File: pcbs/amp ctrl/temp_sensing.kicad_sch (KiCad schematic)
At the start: 8 parts, among them J89 Conn_02x02, U67 ADC081C021

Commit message: Spring connector layout updates
Amp ctrl: added spring connectors for current sense, thermistors, +5V regulator
Amp ctrl: changed pass-through screwdriver holes to mounting holes
Amp ctrl: added part number to optional level shifter
Amp pwr: marked DNP components as DNP
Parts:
- added J116: Conn_01x02, shim:Conn_70AAJ-M_SIB_1x02_P2.54mm_F_bare, symbol Connector_Generic:Conn_01x02
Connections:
- net at C205.2, C207.2, J89.4 (Pin_4)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: now also J116.2 (Pin_2)
- net at C206.2, J89.2 (Pin_2), R267.1: now also J116.1 (Pin_1)
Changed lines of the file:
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@@
 		(exclude_from_sim no)
 		(at 106.68 133.35 0)
-		(size 83.82 27.94)
+		(size 83.82 30.5285)
 		(margins 0.9525 0.9525 0.9525 0.9525)
 		(stroke
@@
 	)
 	(junction
+		(at 100.33 95.25)
+		(diameter 0)
+		(color 0 0 0 0)
+	)
+	(junction
 		(at 181.61 77.47)
 		(diameter 0)
@@
 	)
 	(junction
+		(at 97.79 92.71)
+		(diameter 0)
+		(color 0 0 0 0)
+	)
+	(junction
 		(at 127 95.25)
 		(diameter 0)
@@
 	(wire
 		(pts
-			(xy 93.98 92.71) (xy 127 92.71)
+			(xy 91.44 101.6) (xy 97.79 101.6)
+		)
+		(stroke
+			(width 0)
+			(type default)
+		)
+	)
+	(wire
+		(pts
+			(xy 93.98 92.71) (xy 97.79 92.71)
 		)
 		(stroke
@@
 		)
 	)
+	(wire
+		(pts
+			(xy 97.79 101.6) (xy 97.79 92.71)
+		)
+		(stroke
+			(width 0)
+			(type default)
+		)
+	)
+	(wire
+		(pts
+			(xy 100.33 95.25) (xy 127 95.25)
+		)
+		(stroke
+			(width 0)
+			(type default)
+		)
+	)
 	(polyline
 		(pts
@@
 	(wire
 		(pts
-			(xy 93.98 95.25) (xy 127 95.25)
+			(xy 93.98 95.25) (xy 100.33 95.25)
 		)
 		(stroke
@@
 	(wire
 		(pts
+			(xy 100.33 104.14) (xy 100.33 95.25)
+		)
+		(stroke
+			(width 0)
+			(type default)
+		)
+	)
+	(wire
+		(pts
 			(xy 181.61 77.47) (xy 181.61 76.2)
 		)
@@
 		(pts
 			(xy 142.24 102.87) (xy 142.24 116.84)
+		)
+		(stroke
+			(width 0)
+			(type default)
+		)
+	)
+	(wire
+		(pts
+			(xy 91.44 104.14) (xy 100.33 104.14)
+		)
+		(stroke
+			(width 0)
+			(type default)
+		)
+	)
+	(wire
+		(pts
+			(xy 97.79 92.71) (xy 127 92.71)
 		)
 		(stroke
@@
 					(unit 1)
 				)
+			)
+		)
+	)
+	(symbol
+		(lib_id "Connector_Generic:Conn_01x02")
+		(at 86.36 101.6 0)
+		(mirror y)
+		(unit 1)
+		(body_style 1)
+		(exclude_from_sim no)
+		(in_bom no)
+		(on_board yes)
+		(in_pos_files no)
+		(dnp no)
+		(property "Reference" "J116"
+			(at 83.82 101.5999 0)
+			(show_name no)
+			(do_not_autoplace no)
+			(effects
+				(font
+					(size 1.27 1.27)
+				)
+				(justify left)
+			)
+		)
+		(property "Value" "Conn_01x02"
+			(at 83.82 104.1399 0)
+			(hide yes)
+			(show_name no)
+			(do_not_autoplace no)
+			(effects
+				(font
+					(size 1.27 1.27)
+				)
+				(justify left)
+			)
+		)
+		(property "Footprint" "shim:Conn_70AAJ-M_SIB_1x02_P2.54mm_F_bare"
+			(at 86.36 101.6 0)
+			(hide yes)
+			(show_name no)
+			(do_not_autoplace no)
+			(effects
+				(font
+					(size 1.27 1.27)
+				)
+			)
+		)
+		(property "Datasheet" ""
+			(at 86.36 101.6 0)
+			(hide yes)
+			(show_name no)
+			(do_not_autoplace no)
+			(effects
+				(font
+					(size 1.27 1.27)
+				)
+			)
+		)
+		(property "Description" "Generic connector, single row, 01x02, script generated (kicad-library-utils/schlib/autogen/connector/)"
+			(at 86.36 101.6 0)
+			(hide yes)
+			(show_name no)
+			(do_not_autoplace no)
+			(effects
+				(font
+					(size 1.27 1.27)
+				)
+			)
+		)
+		(pin "1"
+		)
+		(pin "2"
+		)
+		(instances
+			(project "amp ctrl"
+				(path "/00d85075-94bd-47a5-8ecf-5b7663485c5b/00000000-0000-0000-0000-0000614c90a0"
+					(reference "J116")
+					(unit 1)
+				)
+				(path "/00d85075-94bd-47a5-8ecf-5b7663485c5b/00000000-0000-0000-0000-00006152de65"
+					(reference "J117")
+					(unit 1)
+				)
+				(path "/00d85075-94bd-47a5-8ecf-5b7663485c5b/00000000-0000-0000-0000-00006153fab1"
+					(reference "J118")
+					(unit 1)
+				)

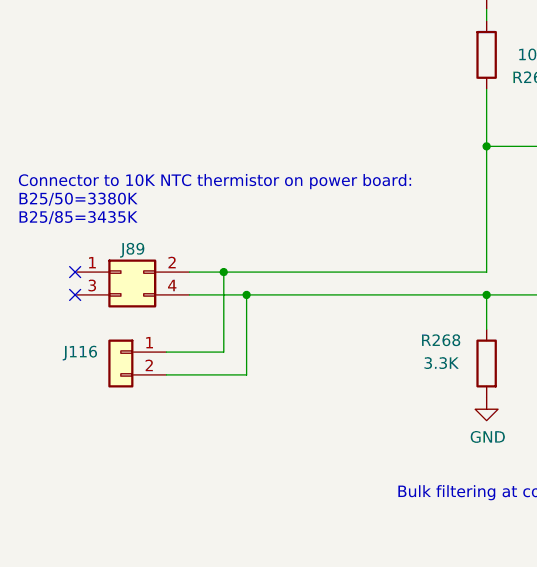
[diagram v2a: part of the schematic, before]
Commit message: Amp ctrl layout for spring pins
Copied layout to all channels & cleaned up inter-channel routing
Updated footprints to latest copies from libraries
Added new SOT-563 footprint for wider clearance between pads, as KiCAD library now has boundary-pushing 0.15 mm (vs. 0.2 mm recc. in 2N7002 datasheet)
Fixed DRC errors
Marked former inter-board connectors (now alternates for spring pins) as DNP
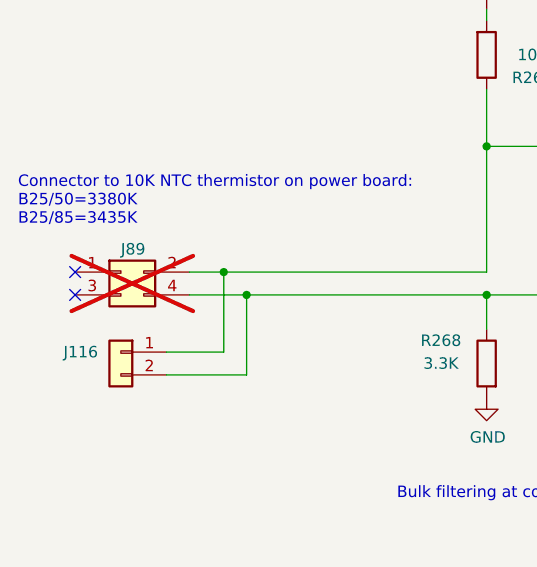
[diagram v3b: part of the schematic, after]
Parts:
- J89: now not fitted
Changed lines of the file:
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@@
 		(on_board yes)
 		(in_pos_files yes)
-		(dnp no)
+		(dnp yes)
 		(property "Reference" "J89"
 			(at 86.36 90.17 0)
